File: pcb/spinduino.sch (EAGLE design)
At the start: 30 parts

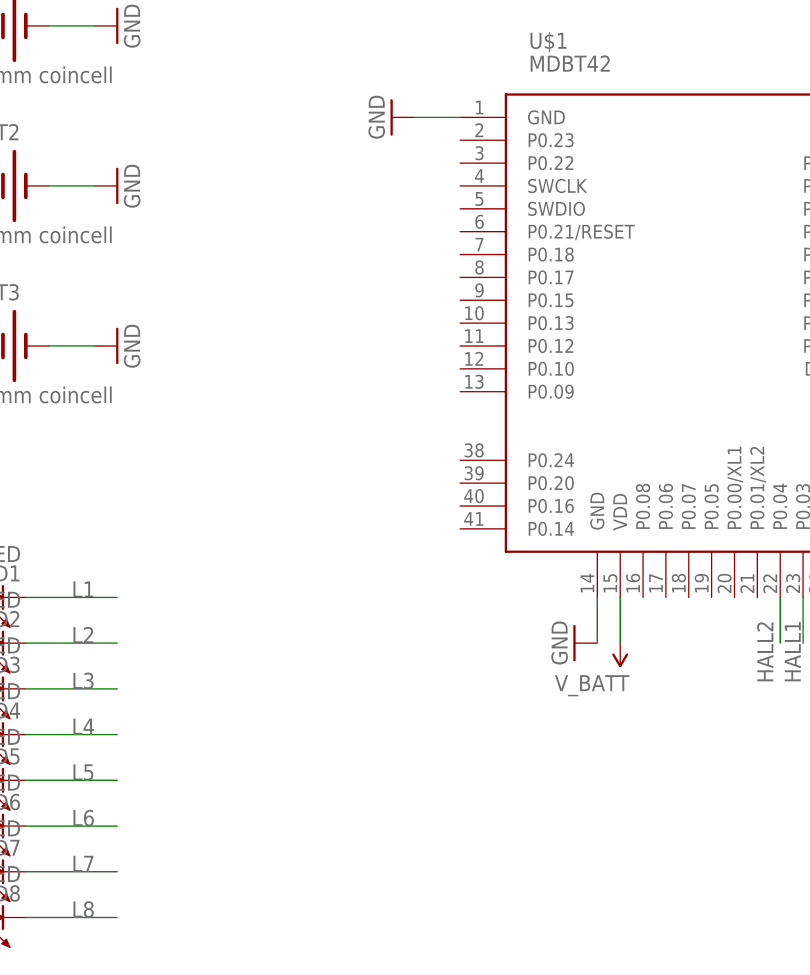
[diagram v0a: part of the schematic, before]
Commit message: add programming connector
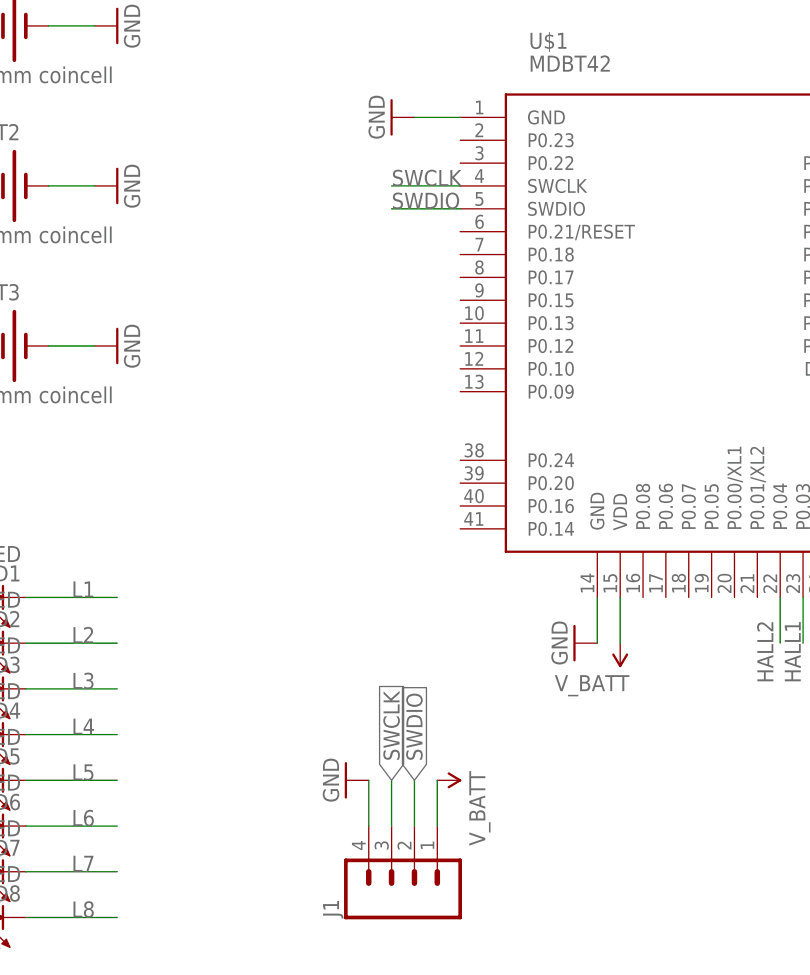
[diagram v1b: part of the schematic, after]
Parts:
- added J1: (no value), ng-beacon:M04LOCK
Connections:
- new net SWCLK: J1.3, U$1.SWCLK
- new net SWDIO: J1.2, U$1.SWDIO
- net GND: now also J1.4
- net V_BATT: now also J1.1
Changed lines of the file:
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@@
 <part name="GND8" library="ng-beacon" deviceset="GND" device=""/>
 <part name="SUPPLY7" library="SparkFun-Aesthetics" deviceset="V_BATT" device=""/>
+<part name="J1" library="ng-beacon" deviceset="M04" device="LOCK"/>
+<part name="GND11" library="ng-beacon" deviceset="GND" device=""/>
+<part name="SUPPLY8" library="SparkFun-Aesthetics" deviceset="V_BATT" device=""/>
 </parts>
 <sheets>
@@
 <instance part="GND8" gate="1" x="43.18" y="111.76" rot="R90"/>
 <instance part="SUPPLY7" gate="G$1" x="22.86" y="111.76" rot="R90"/>
+<instance part="J1" gate="G$1" x="45.72" y="-2.54" rot="R90"/>
+<instance part="GND11" gate="1" x="38.1" y="7.62" rot="R270"/>
+<instance part="SUPPLY8" gate="G$1" x="48.26" y="7.62" rot="R270"/>
 </instances>
 <busses>
@@
 <junction x="38.1" y="111.76"/>
 </segment>
+<segment>
+<pinref part="GND11" gate="1" pin="GND"/>
+<pinref part="J1" gate="G$1" pin="4"/>
+<wire x1="40.64" y1="7.62" x2="40.64" y2="2.54" width="0.1524" layer="91"/>
+</segment>
 </net>
 <net name="L1" class="0">
@@
 <wire x1="25.4" y1="104.14" x2="27.94" y2="104.14" width="0.1524" layer="91"/>
 </segment>
-</net>
+<segment>
+<pinref part="SUPPLY8" gate="G$1" pin="V_BATT"/>
+<pinref part="J1" gate="G$1" pin="1"/>
+<wire x1="48.26" y1="7.62" x2="48.26" y2="2.54" width="0.1524" layer="91"/>
+</segment>
+</net>
+<net name="SWCLK" class="0">
+<segment>
+<pinref part="U$1" gate="G$1" pin="SWCLK"/>
+<wire x1="50.8" y1="73.66" x2="43.18" y2="73.66" width="0.1524" layer="91"/>
+<label x="43.18" y="73.66" size="1.778" layer="95"/>
+</segment>
+<segment>
+<pinref part="J1" gate="G$1" pin="3"/>
+<wire x1="43.18" y1="2.54" x2="43.18" y2="7.62" width="0.1524" layer="91"/>
+<label x="43.18" y="7.62" size="1.778" layer="95" rot="R90" xref="yes"/>
+</segment>
+</net>
+<net name="SWDIO" class="0">
+<segment>
+<pinref part="U$1" gate="G$1" pin="SWDIO"/>
+<wire x1="50.8" y1="71.12" x2="43.18" y2="71.12" width="0.1524" layer="91"/>
+<label x="43.18" y="71.12" size="1.778" layer="95"/>
+</segment>
+<segment>
+<pinref part="J1" gate="G$1" pin="2"/>
+<wire x1="45.72" y1="2.54" x2="45.72" y2="7.62" width="0.1524" layer="91"/>
+<label x="45.72" y="7.62" size="1.778" layer="95" rot="R90" xref="yes"/>
+</segment>
+</net>
